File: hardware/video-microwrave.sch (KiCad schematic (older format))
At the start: 5 parts, among them P101 CONN_01X05, P102 CONN_01X05, P103 CONN_01X05, P104 CONN_01X05, U101 Raspberry_Pi_Zero

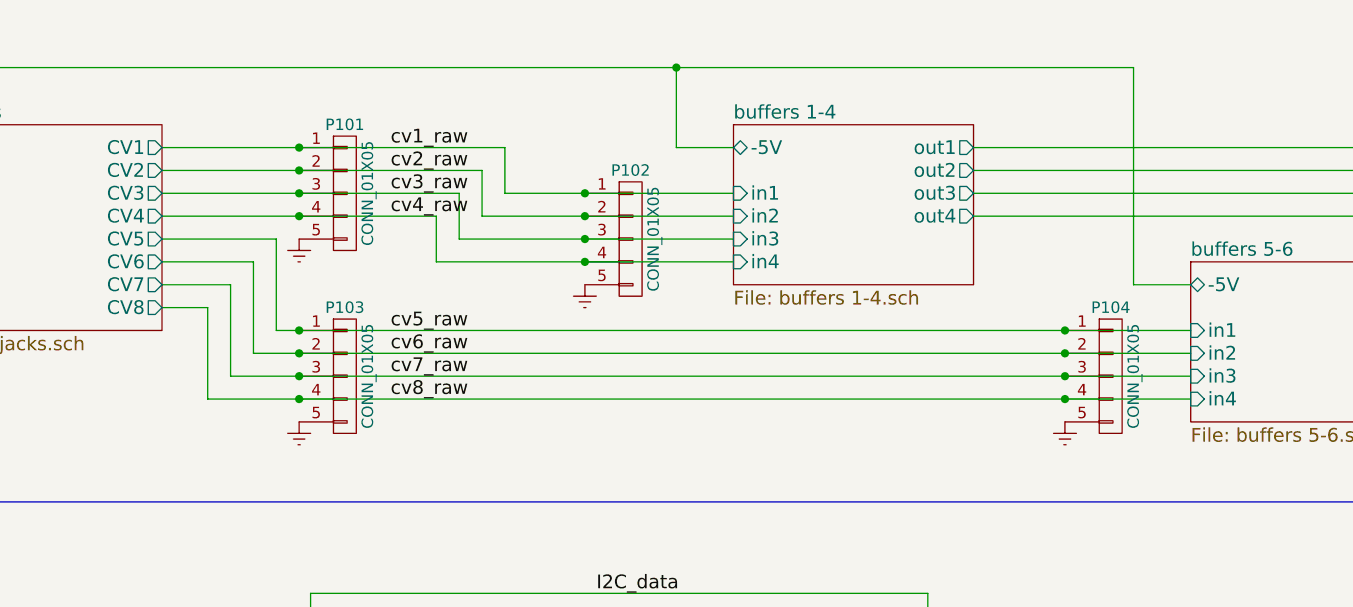
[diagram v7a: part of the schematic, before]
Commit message: moving footprints to fit real world dimensions
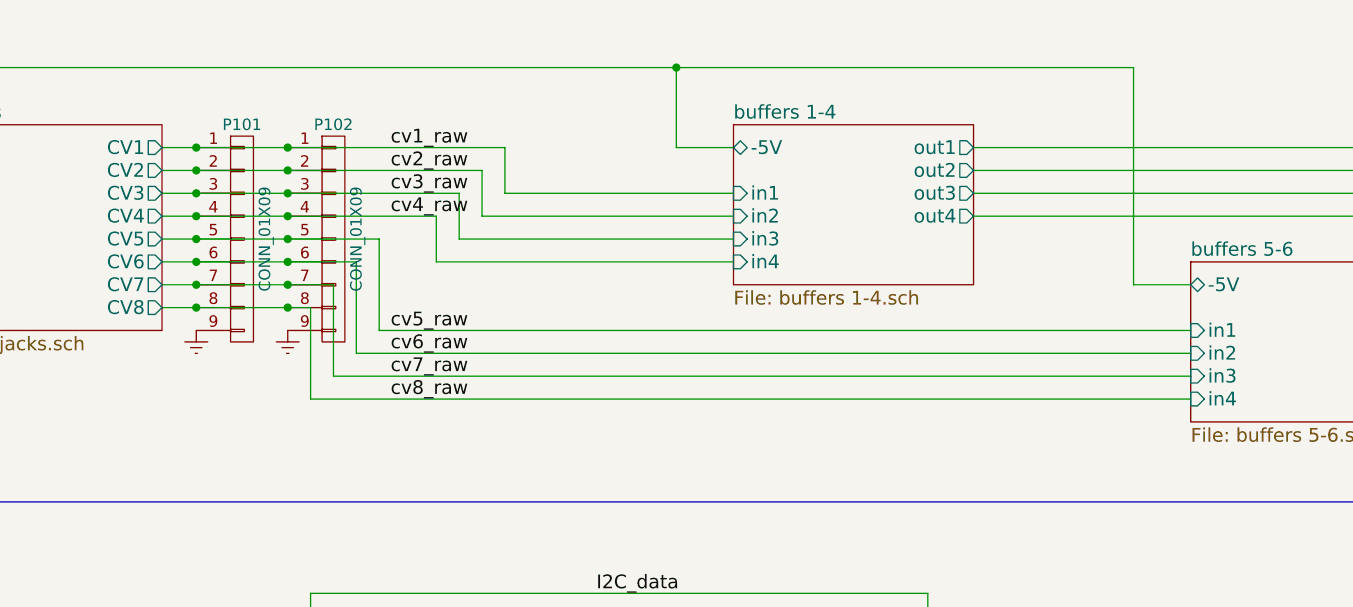
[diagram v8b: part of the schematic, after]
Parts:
- removed P101, P102, P103, P104: CONN_01X05, Pin_Headers:Pin_Header_Straight_1x05_Pitch2.54mm, symbol CONN_01X05
- added P101: CONN_01X09, Pin_Headers:Pin_Header_Angled_1x09_Pitch2.54mm, symbol CONN_01X09
- added P102: CONN_01X09, Pin_Headers:Pin_Header_Straight_1x09_Pitch2.54mm, symbol CONN_01X09
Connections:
- net Earth: now also P101.9 (P9), P102.9 (P9)
- net cv1_raw: now also P101.1 (P1), P102.1 (P1)
- net cv2_raw: now also P101.2 (P2), P102.2 (P2)
- net cv3_raw: now also P101.3 (P3), P102.3 (P3)
- net cv4_raw: now also P101.4 (P4), P102.4 (P4)
- net cv5_raw: now also P101.5 (P5), P102.5 (P5)
- net cv6_raw: now also P101.6 (P6), P102.6 (P6)
- net cv7_raw: now also P101.7 (P7), P102.7 (P7)
- net cv8_raw: now also P101.8 (P8), P102.8 (P8)
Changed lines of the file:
@@
 F10 "in4" I L 8400 2450 60
 $EndSheet
-$Comp
-L CONN_01X05 P101
-U 1 1 5BE59E5A
-P 4700 1550
-F 0 "P101" H 4700 1850 50  0000 C CNN
-F 1 "CONN_01X05" V 4800 1550 50  0000 C CNN
-F 2 "Pin_Headers:Pin_Header_Straight_1x05_Pitch2.54mm" H 4700 1550 50  0001 C CNN
-F 3 "" H 4700 1550 50  0000 C CNN
-	1    4700 1550
-	1    0    0    -1
-$EndComp
-$Comp
-L CONN_01X05 P103
-U 1 1 5BE5A799
-P 4700 2350
-F 0 "P103" H 4700 2650 50  0000 C CNN
-F 1 "CONN_01X05" V 4800 2350 50  0000 C CNN
-F 2 "Pin_Headers:Pin_Header_Straight_1x05_Pitch2.54mm" H 4700 2350 50  0001 C CNN
-F 3 "" H 4700 2350 50  0000 C CNN
-	1    4700 2350
-	1    0    0    -1
-$EndComp
-$Comp
-L CONN_01X05 P102
-U 1 1 5BE5A866
-P 5950 1750
-F 0 "P102" H 5950 2050 50  0000 C CNN
-F 1 "CONN_01X05" V 6050 1750 50  0000 C CNN
-F 2 "Pin_Headers:Pin_Header_Straight_1x05_Pitch2.54mm" H 5950 1750 50  0001 C CNN
-F 3 "" H 5950 1750 50  0000 C CNN
-	1    5950 1750
-	1    0    0    -1
-$EndComp
-$Comp
-L CONN_01X05 P104
-U 1 1 5BE5A932
-P 8050 2350
-F 0 "P104" H 8050 2650 50  0000 C CNN
-F 1 "CONN_01X05" V 8150 2350 50  0000 C CNN
-F 2 "Pin_Headers:Pin_Header_Straight_1x05_Pitch2.54mm" H 8050 2350 50  0001 C CNN
-F 3 "" H 8050 2350 50  0000 C CNN
-	1    8050 2350
-	1    0    0    -1
-$EndComp
 Wire Wire Line
 	3900 1350 5400 1350
@@
 Wire Wire Line
 	5400 1550 6400 1550
-Connection ~ 4500 1350
-Connection ~ 5750 1550
+Connection ~ 4050 1350
+Connection ~ 4450 1350
 Wire Wire Line
 	3900 1450 5300 1450
@@
 Wire Wire Line
 	5300 1650 6400 1650
-Connection ~ 4500 1450
-Connection ~ 5750 1650
+Connection ~ 4050 1450
+Connection ~ 4450 1450
 Wire Wire Line
 	3900 1550 5200 1550
@@
 Wire Wire Line
 	5200 1750 6400 1750
-Connection ~ 4500 1550
-Connection ~ 5750 1750
+Connection ~ 4050 1550
+Connection ~ 4450 1550
 Wire Wire Line
 	3900 1650 5100 1650
@@
 Wire Wire Line
 	5100 1850 6400 1850
-Connection ~ 4500 1650
-Connection ~ 5750 1850
-Wire Wire Line
-	4400 2150 8400 2150
-Wire Wire Line
-	4300 2250 8400 2250
-Wire Wire Line
-	4200 2350 8400 2350
-Wire Wire Line
-	4100 2450 8400 2450
-Wire Wire Line
-	3900 1750 4400 1750
-Wire Wire Line
-	4400 1750 4400 2150
-Connection ~ 4500 2150
-Wire Wire Line
-	3900 1850 4300 1850
-Wire Wire Line
-	4300 1850 4300 2250
-Connection ~ 4500 2250
-Wire Wire Line
-	3900 1950 4200 1950
-Wire Wire Line
-	4200 1950 4200 2350
-Connection ~ 4500 2350
-Wire Wire Line
-	3900 2050 4100 2050
-Wire Wire Line
-	4100 2050 4100 2450
-Connection ~ 4500 2450
-Connection ~ 7850 2450
-Connection ~ 7850 2350
-Connection ~ 7850 2250
-Connection ~ 7850 2150
+Connection ~ 4050 1650
+Connection ~ 4450 1650
+Wire Wire Line
+	4850 2150 8400 2150
+Wire Wire Line
+	4750 2250 8400 2250
+Wire Wire Line
+	4650 2350 8400 2350
+Wire Wire Line
+	4550 2450 8400 2450
+Wire Wire Line
+	3900 1750 4850 1750
+Wire Wire Line
+	4850 1750 4850 2150
+Connection ~ 4050 1750
+Wire Wire Line
+	3900 1850 4750 1850
+Wire Wire Line
+	4750 1850 4750 2250
+Connection ~ 4050 1850
+Wire Wire Line
+	3900 1950 4650 1950
+Wire Wire Line
+	4650 1950 4650 2350
+Connection ~ 4050 1950
+Wire Wire Line
+	3900 2050 4550 2050
+Wire Wire Line
+	4550 2050 4550 2450
+Connection ~ 4050 2050
 $Comp
 L Earth #PWR04
-U 1 1 5BE5E4CE
-P 4500 1750
-F 0 "#PWR04" H 4500 1500 50  0001 C CNN
-F 1 "Earth" H 4500 1600 50  0001 C CNN
-F 2 "" H 4500 1750 50  0000 C CNN
-F 3 "" H 4500 1750 50  0000 C CNN
-	1    4500 1750
-	1    0    0    -1
-$EndComp
-$Comp
-L Earth #PWR05
 U 1 1 5BE5E7A4
-P 4500 2550
-F 0 "#PWR05" H 4500 2300 50  0001 C CNN
-F 1 "Earth" H 4500 2400 50  0001 C CNN
-F 2 "" H 4500 2550 50  0000 C CNN
-F 3 "" H 4500 2550 50  0000 C CNN
-	1    4500 2550
-	1    0    0    -1
-$EndComp
-$Comp
-L Earth #PWR06
-U 1 1 5BE5E860
-P 5750 1950
-F 0 "#PWR06" H 5750 1700 50  0001 C CNN
-F 1 "Earth" H 5750 1800 50  0001 C CNN
-F 2 "" H 5750 1950 50  0000 C CNN
-F 3 "" H 5750 1950 50  0000 C CNN
-	1    5750 1950
-	1    0    0    -1
-$EndComp
-$Comp
-L Earth #PWR07
-U 1 1 5BE5EE26
-P 7850 2550
-F 0 "#PWR07" H 7850 2300 50  0001 C CNN
-F 1 "Earth" H 7850 2400 50  0001 C CNN
-F 2 "" H 7850 2550 50  0000 C CNN
-F 3 "" H 7850 2550 50  0000 C CNN
-	1    7850 2550
+P 4450 2150
+F 0 "#PWR04" H 4450 1900 50  0001 C CNN
+F 1 "Earth" H 4450 2000 50  0001 C CNN
+F 2 "" H 4450 2150 50  0000 C CNN
+F 3 "" H 4450 2150 50  0000 C CNN
+	1    4450 2150
 	1    0    0    -1
 $EndComp
@@
 Text Label 4900 2450 0    60   ~ 0
 cv8_raw
+$Comp
+L CONN_01X09 P101
+U 1 1 5C00105D
+P 4250 1750
+F 0 "P101" H 4250 2250 50  0000 C CNN
+F 1 "CONN_01X09" V 4350 1750 50  0000 C CNN
+F 2 "Pin_Headers:Pin_Header_Angled_1x09_Pitch2.54mm" H 4250 1750 50  0001 C CNN
+F 3 "" H 4250 1750 50  0000 C CNN
+	1    4250 1750
+	1    0    0    -1
+$EndComp
+$Comp
+L CONN_01X09 P102
+U 1 1 5C006237
+P 4650 1750
+F 0 "P102" H 4650 2250 50  0000 C CNN
+F 1 "CONN_01X09" V 4750 1750 50  0000 C CNN
+F 2 "Pin_Headers:Pin_Header_Straight_1x09_Pitch2.54mm" H 4650 1750 50  0001 C CNN
+F 3 "" H 4650 1750 50  0000 C CNN
+	1    4650 1750
+	1    0    0    -1
+$EndComp
+Connection ~ 4450 1750
+Connection ~ 4450 1850
+Connection ~ 4450 1950
+Connection ~ 4450 2050
+$Comp
+L Earth #PWR05
+U 1 1 5C006D7A
+P 4050 2150
+F 0 "#PWR05" H 4050 1900 50  0001 C CNN
+F 1 "Earth" H 4050 2000 50  0001 C CNN
+F 2 "" H 4050 2150 50  0000 C CNN
+F 3 "" H 4050 2150 50  0000 C CNN
+	1    4050 2150
+	1    0    0    -1
+$EndComp
 $EndSCHEMATC
